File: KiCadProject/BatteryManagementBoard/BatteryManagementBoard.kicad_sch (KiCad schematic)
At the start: 0 parts

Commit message: BQ25713 and LDO done? Stm32 next I think
Signed-off-by: Eldalote.Electronics <Eldalote.Electronics@gmail.com>
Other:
- added sheet P6 - 3V3 Regulator (P6LPregulator.kicad_sch)

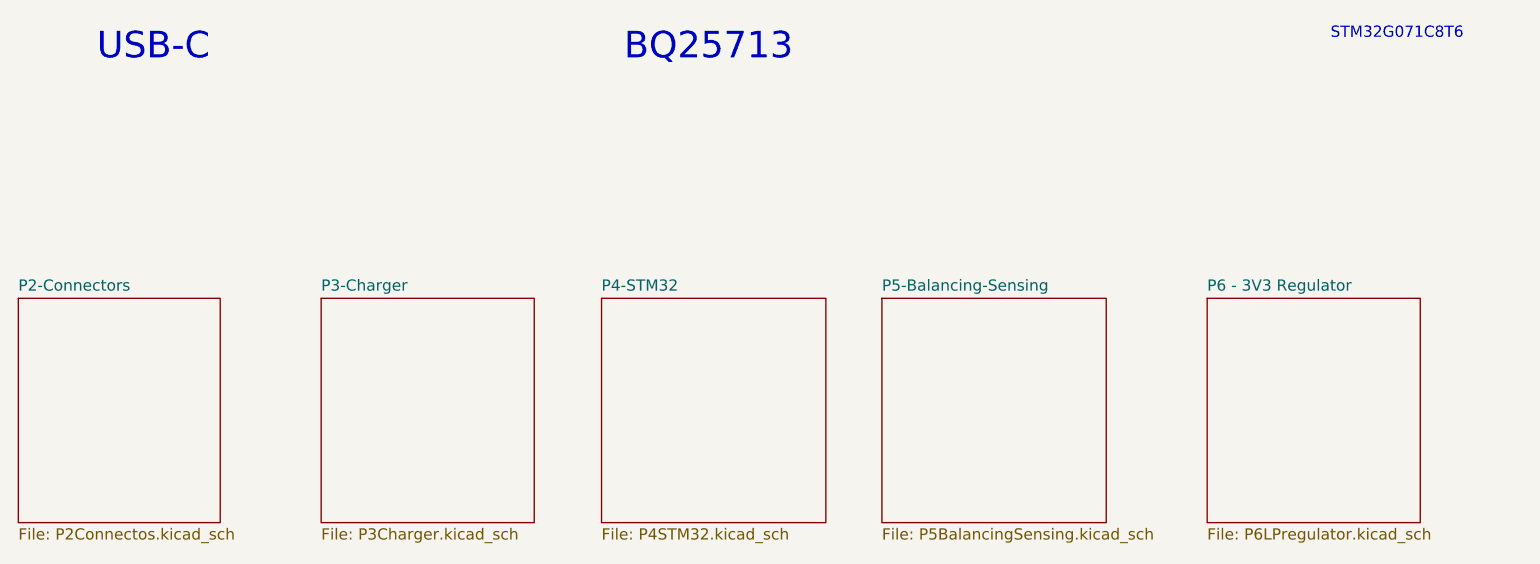
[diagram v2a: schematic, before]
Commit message: Change to design: No more STM32, just use resistors for USB-C PD, en move the battery cell measuring and leveling to the other board.
Signed-off-by: Eldalote.Electronics <Eldalote.Electronics@gmail.com>
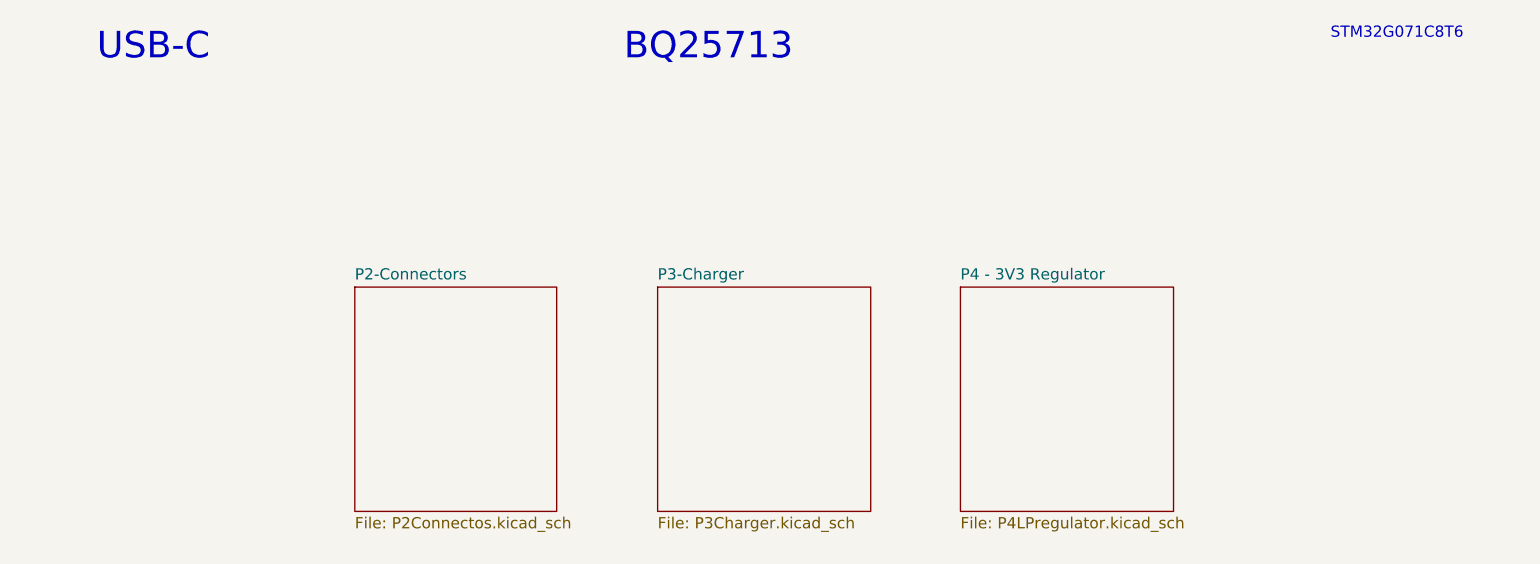
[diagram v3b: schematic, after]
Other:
- sheet P6 - 3V3 Regulator renamed P4 - 3V3 Regulator
- removed sheet P4-STM32
- removed sheet P5-Balancing-Sensing
- sheet P4 - 3V3 Regulator: file P6LPregulator.kicad_sch -> P4LPregulator.kicad_sch
- company: (none) -> Eldalote Electronics

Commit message: jan 4
Signed-off-by: Eldalote.Electronics <Eldalote.Electronics@gmail.com>
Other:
- added sheet P5-TUSB422 (Optional) (P5TUSB422.kicad_sch)

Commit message: Tweaking
Signed-off-by: Eldalote.Electronics <Eldalote.Electronics@gmail.com>
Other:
- note removed: "STM32G071C8T6"
